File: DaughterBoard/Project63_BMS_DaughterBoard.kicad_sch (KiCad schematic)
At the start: 0 parts

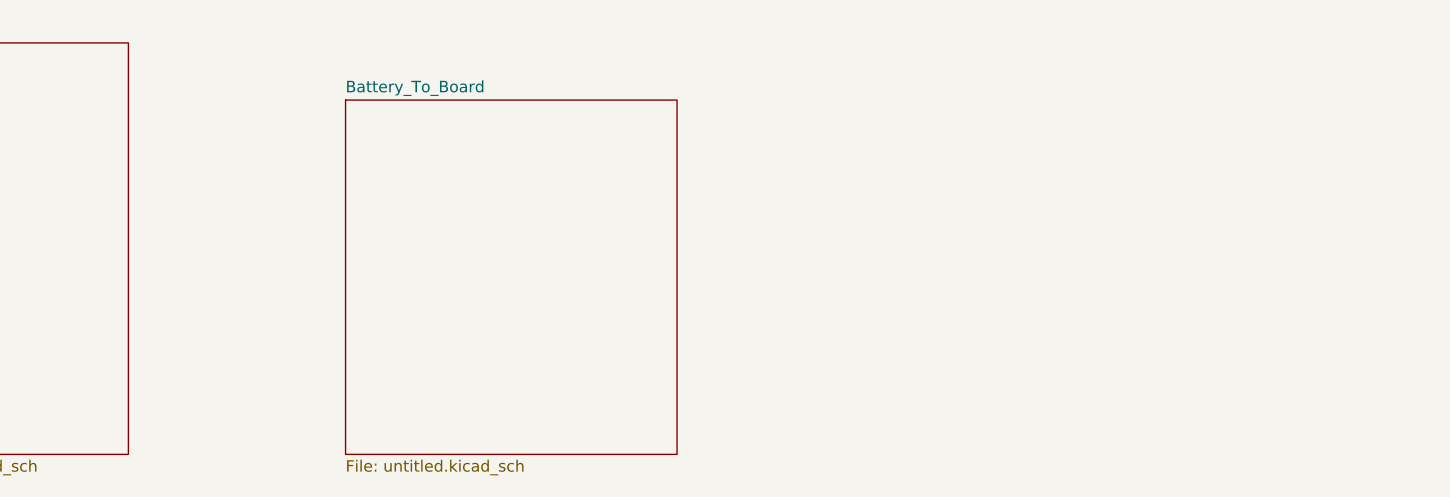
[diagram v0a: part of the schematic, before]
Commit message: Add files via upload
Updated KiCAD schematics for Daughter Board. (10/10/24)
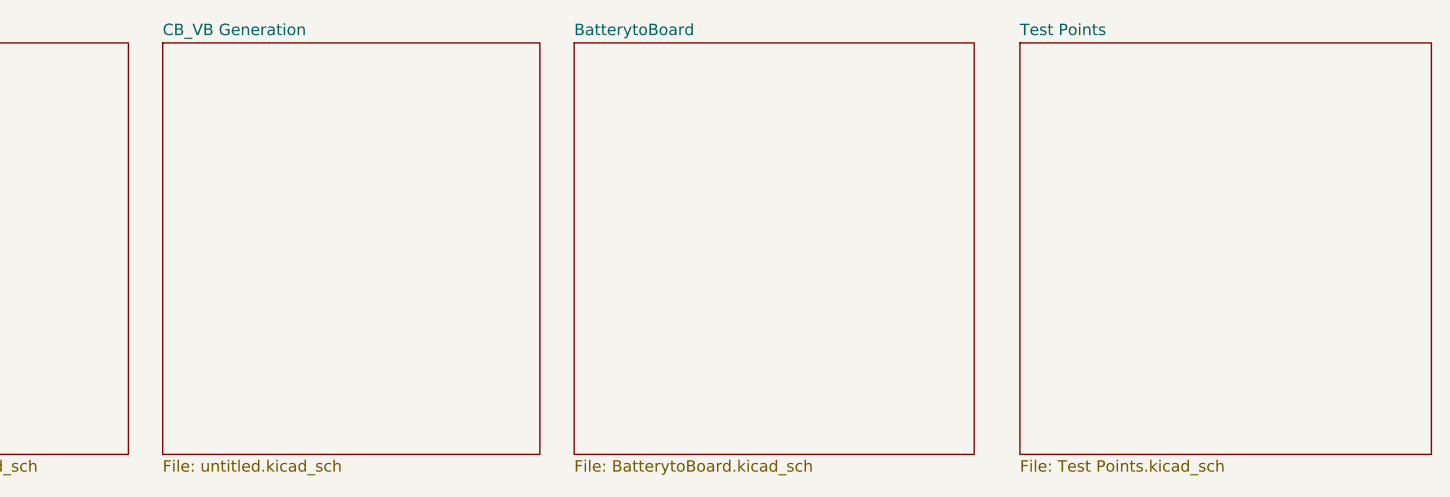
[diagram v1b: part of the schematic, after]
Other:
- sheet Battery_To_Board renamed CB_VB Generation
- added sheet BatterytoBoard (BatterytoBoard.kicad_sch)
- added sheet Test Points (Test Points.kicad_sch)
- title: (none) -> Project 63 BMS Daughter Board
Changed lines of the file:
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@@
 	(generator_version "8.0")
 	(paper "A4")
+	(title_block
+		(title "Project 63 BMS Daughter Board")
+	)
 	(sheet
-		(at 93.98 29.21)
-		(size 36.83 39.37)
+		(at 73.66 22.86)
+		(size 41.91 45.72)
 		(fields_autoplaced yes)
 		(stroke
@@
 			(color 0 0 0 0.0000)
 		)
-		(property "Sheetname" "Battery_To_Board"
-			(at 93.98 28.4984 0)
+		(property "Sheetname" "CB_VB Generation"
+			(at 73.66 22.1484 0)
 			(effects
 				(font
@@
 		)
 		(property "Sheetfile" "untitled.kicad_sch"
-			(at 93.98 69.1646 0)
+			(at 73.66 69.1646 0)
 			(effects
 				(font
@@
 				(path "/325b096d-8e4c-4cdc-b4c5-634ea5e73c60"
 					(page "3")
+				)
+			)
+		)
+	)
+	(sheet
+		(at 119.38 22.86)
+		(size 44.45 45.72)
+		(fields_autoplaced yes)
+		(stroke
+			(width 0.1524)
+			(type solid)
+		)
+		(fill
+			(color 0 0 0 0.0000)
+		)
+		(property "Sheetname" "BatterytoBoard"
+			(at 119.38 22.1484 0)
+			(effects
+				(font
+					(size 1.27 1.27)
+				)
+				(justify left bottom)
+			)
+		)
+		(property "Sheetfile" "BatterytoBoard.kicad_sch"
+			(at 119.38 69.1646 0)
+			(effects
+				(font
+					(size 1.27 1.27)
+				)
+				(justify left top)
+			)
+		)
+		(instances
+			(project "Project63_BMS_DaughterBoard"
+				(path "/325b096d-8e4c-4cdc-b4c5-634ea5e73c60"
+					(page "4")
 				)
 			)
@@
 				)
 			)
+		)
+	)
+	(sheet
+		(at 168.91 22.86)
+		(size 45.72 45.72)
+		(fields_autoplaced yes)
+		(stroke
+			(width 0.1524)
+			(type solid)
+		)
+		(fill
+			(color 0 0 0 0.0000)
+		)
+		(property "Sheetname" "Test Points"
+			(at 168.91 22.1484 0)
+			(effects
+				(font
+					(size 1.27 1.27)
+				)
+				(justify left bottom)
+			)
+		)
+		(property "Sheetfile" "Test Points.kicad_sch"
+			(at 168.91 69.1646 0)
+			(effects
+				(font
+					(size 1.27 1.27)
+				)
+				(justify left top)
+			)
+		)
+		(instances
+			(project "Project63_BMS_DaughterBoard"
+				(path "/325b096d-8e4c-4cdc-b4c5-634ea5e73c60"
+					(page "5")
+				)
+			)

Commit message: modhy commit
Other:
- added sheet NPN Power Supply (NPN Power Supply.kicad_sch)
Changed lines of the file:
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@@
+	)
+	(sheet
+		(at 219.71 22.86)
+		(size 50.8 46.99)
+		(fields_autoplaced yes)
+		(stroke
+			(width 0.1524)
+			(type solid)
+		)
+		(fill
+			(color 0 0 0 0.0000)
+		)
+		(property "Sheetname" "NPN Power Supply"
+			(at 219.71 22.1484 0)
+			(effects
+				(font
+					(size 1.27 1.27)
+				)
+				(justify left bottom)
+			)
+		)
+		(property "Sheetfile" "NPN Power Supply.kicad_sch"
+			(at 219.71 70.4346 0)
+			(effects
+				(font
+					(size 1.27 1.27)
+				)
+				(justify left top)
+			)
+		)
+		(instances
+			(project "Project63_BMS_DaughterBoard"
+				(path "/325b096d-8e4c-4cdc-b4c5-634ea5e73c60"
+					(page "6")
+				)
+			)
+		)
 	)
 	(sheet

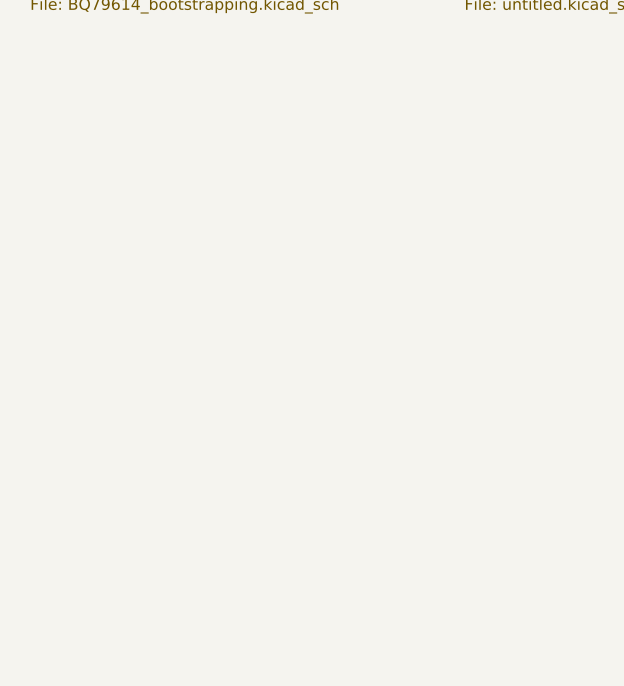
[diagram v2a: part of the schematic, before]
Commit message: I think all componets for DOBO schematic are added, wired and assigned to their footprints. Next step to work on ERC
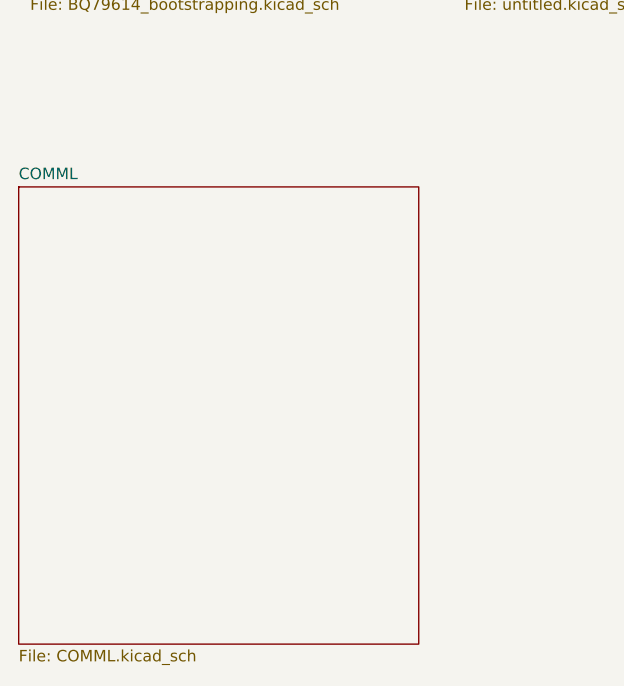
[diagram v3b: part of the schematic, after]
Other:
- added sheet COMML (COMML.kicad_sch)
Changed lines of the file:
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@@
+	)
+	(sheet
+		(at 24.13 90.17)
+		(size 44.45 50.8)
+		(fields_autoplaced yes)
+		(stroke
+			(width 0.1524)
+			(type solid)
+		)
+		(fill
+			(color 0 0 0 0.0000)
+		)
+		(property "Sheetname" "COMML"
+			(at 24.13 89.4584 0)
+			(effects
+				(font
+					(size 1.27 1.27)
+				)
+				(justify left bottom)
+			)
+		)
+		(property "Sheetfile" "COMML.kicad_sch"
+			(at 24.13 141.5546 0)
+			(effects
+				(font
+					(size 1.27 1.27)
+				)
+				(justify left top)
+			)
+		)
+		(instances
+			(project "Project63_BMS_DaughterBoard"
+				(path "/325b096d-8e4c-4cdc-b4c5-634ea5e73c60"
+					(page "7")
+				)
+			)
+		)
 	)
 	(sheet

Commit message: Updates
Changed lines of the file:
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@@
 	)
 	(sheet
-		(at 24.13 90.17)
+		(at 24.765 90.805)
 		(size 44.45 50.8)
 		(fields_autoplaced yes)
@@
 		)
 		(property "Sheetname" "COMML"
-			(at 24.13 89.4584 0)
+			(at 24.765 90.0934 0)
 			(effects
 				(font
@@
 		)
 		(property "Sheetfile" "COMML.kicad_sch"
-			(at 24.13 141.5546 0)
+			(at 24.765 142.1896 0)
 			(effects
 				(font

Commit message: Finished board
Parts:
- added H101, H102, H103, H104: MountingHole, MountingHole:MountingHole_3.2mm_M3, symbol Mechanical:MountingHole

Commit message: Both boards complete
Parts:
- H101, H102, H103, H104: now not fitted
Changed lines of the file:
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@@
 		(in_bom no)
 		(on_board yes)
-		(dnp no)
+		(dnp yes)
 		(fields_autoplaced yes)
 		(property "Reference" "H103"
@@
 		)
 		(property "Description" "Mounting Hole without connection"
+			(at 50.8 165.1 0)
+			(effects
+				(font
+					(size 1.27 1.27)
+				)
+				(hide yes)
+			)
+		)
+		(property "JLC PCB Part #" ""
 			(at 50.8 165.1 0)
 			(effects
@@
 		(in_bom no)
 		(on_board yes)
-		(dnp no)
+		(dnp yes)
 		(fields_autoplaced yes)
 		(property "Reference" "H101"
@@
 		)
 		(property "Description" "Mounting Hole without connection"
+			(at 25.4 165.1 0)
+			(effects
+				(font
+					(size 1.27 1.27)
+				)
+				(hide yes)
+			)
+		)
+		(property "JLC PCB Part #" ""
 			(at 25.4 165.1 0)
 			(effects
@@
 		(in_bom no)
 		(on_board yes)
-		(dnp no)
+		(dnp yes)
 		(fields_autoplaced yes)
 		(property "Reference" "H104"
@@
 		)
 		(property "Description" "Mounting Hole without connection"
+			(at 50.8 177.8 0)
+			(effects
+				(font
+					(size 1.27 1.27)
+				)
+				(hide yes)
+			)
+		)
+		(property "JLC PCB Part #" ""
 			(at 50.8 177.8 0)
 			(effects
@@
 		(in_bom no)
 		(on_board yes)
-		(dnp no)
+		(dnp yes)
 		(fields_autoplaced yes)
 		(property "Reference" "H102"
@@
 			(at 25.4 177.8 0)
 			(effects
+				(font
+					(size 1.27 1.27)
+				)
+				(hide yes)
+			)
+		)
+		(property "JLC PCB Part #" ""
+			(at 25.4 177.8 0)
+			(effects
